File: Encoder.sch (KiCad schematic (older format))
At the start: 7 parts

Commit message: ordenar referencias de componentes
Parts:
- C8, C9: value C -> 1u; Fabricante (none) -> SAMSUNG; Provedor (none) -> TME; Ref (none) -> CL21B105KAFNNNE; Ref_Proveedor (none) -> CL21B105KAFNNNE
- R37: renamed from R36; value R -> 10K; Fabricante (none) -> VISHAY; Potencia (none) -> 1/8W; Provedor (none) -> TME; Ref (none) -> CRCW080510K0FKEA; Ref_Proveedor (none) -> CRCW080510K0FKEA; Tolerancia (none) -> 1%
- R38: renamed from R37; value R -> 10K; Fabricante (none) -> VISHAY; Potencia (none) -> 1/8W; Provedor (none) -> TME; Ref (none) -> CRCW080510K0FKEA; Ref_Proveedor (none) -> CRCW080510K0FKEA; Tolerancia (none) -> 1%
- R39: renamed from R38; value R -> 10K; Fabricante (none) -> VISHAY; Potencia (none) -> 1/8W; Provedor (none) -> TME; Ref (none) -> CRCW080510K0FKEA; Ref_Proveedor (none) -> CRCW080510K0FKEA; Tolerancia (none) -> 1%
- R40: renamed from R39; value R -> 10K; Fabricante (none) -> VISHAY; Potencia (none) -> 1/8W; Provedor (none) -> TME; Ref (none) -> CRCW080510K0FKEA; Ref_Proveedor (none) -> CRCW080510K0FKEA; Tolerancia (none) -> 1%
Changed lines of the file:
@@
 $Descr User 8268 5846
 encoding utf-8
-Sheet 14 15
+Sheet 15 15
 Title ""
 Date ""
@@
 	1600 2450 1600 2750
 $Comp
-L GND #PWR052
+L GND #PWR57
 U 1 1 579DF9A7
 P 1600 2750
-F 0 "#PWR052" H 1600 2500 50  0001 C CNN
+F 0 "#PWR57" H 1600 2500 50  0001 C CNN
 F 1 "GND" H 1605 2577 50  0000 C CNN
 F 2 "" H 1600 2750 50  0000 C CNN
@@
 $EndComp
 $Comp
-L R R36
+L R R37
 U 1 1 579DF9C8
 P 2400 1800
-F 0 "R36" H 2470 1846 50  0000 L CNN
-F 1 "R" H 2470 1755 50  0000 L CNN
+F 0 "R37" H 2470 1846 50  0000 L CNN
+F 1 "10K" H 2470 1755 50  0000 L CNN
 F 2 "Resistors_SMD:R_0805" V 2330 1800 50  0001 C CNN
 F 3 "" H 2400 1800 50  0000 C CNN
+F 4 "VISHAY" H 3950 1650 60  0001 C CNN "Fabricante"
+F 5 "CRCW080510K0FKEA" H 3950 1650 60  0001 C CNN "Ref"
+F 6 "1/8W" H 3950 1650 60  0001 C CNN "Potencia"
+F 7 "1%" H 3950 1650 60  0001 C CNN "Tolerancia"
+F 8 "TME" H 3950 1650 60  0001 C CNN "Provedor"
+F 9 "CRCW080510K0FKEA" H 3950 1650 60  0001 C CNN "Ref_Proveedor"
 	1    2400 1800
 	1    0    0    -1
 $EndComp
 $Comp
-L R R38
+L R R39
 U 1 1 579DFA38
 P 2750 1800
-F 0 "R38" H 2820 1846 50  0000 L CNN
-F 1 "R" H 2820 1755 50  0000 L CNN
+F 0 "R39" H 2820 1846 50  0000 L CNN
+F 1 "10K" H 2820 1755 50  0000 L CNN
 F 2 "Resistors_SMD:R_0805" V 2680 1800 50  0001 C CNN
 F 3 "" H 2750 1800 50  0000 C CNN
+F 4 "VISHAY" H 3950 1650 60  0001 C CNN "Fabricante"
+F 5 "CRCW080510K0FKEA" H 3950 1650 60  0001 C CNN "Ref"
+F 6 "1/8W" H 3950 1650 60  0001 C CNN "Potencia"
+F 7 "1%" H 3950 1650 60  0001 C CNN "Tolerancia"
+F 8 "TME" H 3950 1650 60  0001 C CNN "Provedor"
+F 9 "CRCW080510K0FKEA" H 3950 1650 60  0001 C CNN "Ref_Proveedor"
 	1    2750 1800
 	1    0    0    -1
 $EndComp
 $Comp
-L R R37
+L R R38
 U 1 1 579DFA57
 P 2400 2450
-F 0 "R37" H 2470 2496 50  0000 L CNN
-F 1 "R" H 2470 2405 50  0000 L CNN
+F 0 "R38" H 2470 2496 50  0000 L CNN
+F 1 "10K" H 2470 2405 50  0000 L CNN
 F 2 "Resistors_SMD:R_0805" V 2330 2450 50  0001 C CNN
 F 3 "" H 2400 2450 50  0000 C CNN
+F 4 "VISHAY" H 3950 1650 60  0001 C CNN "Fabricante"
+F 5 "CRCW080510K0FKEA" H 3950 1650 60  0001 C CNN "Ref"
+F 6 "1/8W" H 3950 1650 60  0001 C CNN "Potencia"
+F 7 "1%" H 3950 1650 60  0001 C CNN "Tolerancia"
+F 8 "TME" H 3950 1650 60  0001 C CNN "Provedor"
+F 9 "CRCW080510K0FKEA" H 3950 1650 60  0001 C CNN "Ref_Proveedor"
 	1    2400 2450
 	1    0    0    -1
 $EndComp
 $Comp
-L R R39
+L R R40
 U 1 1 579DFA8F
 P 2750 2450
-F 0 "R39" H 2820 2496 50  0000 L CNN
-F 1 "R" H 2820 2405 50  0000 L CNN
+F 0 "R40" H 2820 2496 50  0000 L CNN
+F 1 "10K" H 2820 2405 50  0000 L CNN
 F 2 "Resistors_SMD:R_0805" V 2680 2450 50  0001 C CNN
 F 3 "" H 2750 2450 50  0000 C CNN
+F 4 "VISHAY" H 3950 1650 60  0001 C CNN "Fabricante"
+F 5 "CRCW080510K0FKEA" H 3950 1650 60  0001 C CNN "Ref"
+F 6 "1/8W" H 3950 1650 60  0001 C CNN "Potencia"
+F 7 "1%" H 3950 1650 60  0001 C CNN "Tolerancia"
+F 8 "TME" H 3950 1650 60  0001 C CNN "Provedor"
+F 9 "CRCW080510K0FKEA" H 3950 1650 60  0001 C CNN "Ref_Proveedor"
 	1    2750 2450
 	1    0    0    -1
@@
 P 2400 3100
 F 0 "C8" H 2515 3146 50  0000 L CNN
-F 1 "C" H 2515 3055 50  0000 L CNN
+F 1 "1u" H 2515 3055 50  0000 L CNN
 F 2 "Capacitors_SMD:C_0805" H 2438 2950 50  0001 C CNN
 F 3 "" H 2400 3100 50  0000 C CNN
+F 4 "SAMSUNG" H 2400 3100 60  0001 C CNN "Fabricante"
+F 5 "CL21B105KAFNNNE" H 2400 3100 60  0001 C CNN "Ref"
+F 6 "~" H 2400 3100 60  0001 C CNN "Potencia"
+F 7 "~" H 2400 3100 60  0001 C CNN "Tolerancia"
+F 8 "TME" H 2400 3100 60  0001 C CNN "Provedor"
+F 9 "CL21B105KAFNNNE" H 2400 3100 60  0001 C CNN "Ref_Proveedor"
 	1    2400 3100
 	1    0    0    -1
@@
 P 2750 3100
 F 0 "C9" H 2865 3146 50  0000 L CNN
-F 1 "C" H 2865 3055 50  0000 L CNN
+F 1 "1u" H 2865 3055 50  0000 L CNN
 F 2 "Capacitors_SMD:C_0805" H 2788 2950 50  0001 C CNN
 F 3 "" H 2750 3100 50  0000 C CNN
+F 4 "SAMSUNG" H 2750 3100 60  0001 C CNN "Fabricante"
+F 5 "CL21B105KAFNNNE" H 2750 3100 60  0001 C CNN "Ref"
+F 6 "~" H 2750 3100 60  0001 C CNN "Potencia"
+F 7 "~" H 2750 3100 60  0001 C CNN "Tolerancia"
+F 8 "TME" H 2750 3100 60  0001 C CNN "Provedor"
+F 9 "CL21B105KAFNNNE" H 2750 3100 60  0001 C CNN "Ref_Proveedor"
 	1    2750 3100
 	1    0    0    -1
@@
 	2400 2600 2400 2950
 $Comp
-L GND #PWR053
+L GND #PWR59
 U 1 1 579DFBCA
 P 2400 3350
-F 0 "#PWR053" H 2400 3100 50  0001 C CNN
+F 0 "#PWR59" H 2400 3100 50  0001 C CNN
 F 1 "GND" H 2405 3177 50  0000 C CNN
 F 2 "" H 2400 3350 50  0000 C CNN
@@
 $EndComp
 $Comp
-L GND #PWR054
+L GND #PWR61
 U 1 1 579DFBEA
 P 2750 3350
-F 0 "#PWR054" H 2750 3100 50  0001 C CNN
+F 0 "#PWR61" H 2750 3100 50  0001 C CNN
 F 1 "GND" H 2755 3177 50  0000 C CNN
 F 2 "" H 2750 3350 50  0000 C CNN
@@
 	2400 3350 2400 3250
 $Comp
-L +5V #PWR055
+L +5V #PWR58
 U 1 1 579DFC2A
 P 2400 1450
-F 0 "#PWR055" H 2400 1300 50  0001 C CNN
+F 0 "#PWR58" H 2400 1300 50  0001 C CNN
 F 1 "+5V" H 2415 1623 50  0000 C CNN
 F 2 "" H 2400 1450 50  0000 C CNN
@@
 $EndComp
 $Comp
-L +5V #PWR056
+L +5V #PWR60
 U 1 1 579DFC51
 P 2750 1450
-F 0 "#PWR056" H 2750 1300 50  0001 C CNN
+F 0 "#PWR60" H 2750 1300 50  0001 C CNN
 F 1 "+5V" H 2765 1623 50  0000 C CNN
 F 2 "" H 2750 1450 50  0000 C CNN

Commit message: cambiados encoder y potenciometro
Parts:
- B1: footprint Sensores:Bourns_3315C_encoder_incremental -> Sensores:ALPS_EC12E24_encoder_incremental; Fabricante Bourns -> ALPS; Ref 3315C-101-016L -> EC12E24202A2; Ref_Proveedor 827-5019 -> 623-4215
- R37, R38, R39, R40: footprint Resistors_SMD:R_0805 -> Resistencias:R_0805
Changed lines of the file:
@@
 F 0 "B1" H 1656 2877 100 0000 C CNN
 F 1 "Encoder_Inc" H 1656 2711 100 0000 C CNN
-F 2 "Sensores:Bourns_3315C_encoder_incremental" H 1450 2250 100 0001 C CNN
+F 2 "Sensores:ALPS_EC12E24_encoder_incremental" H 1450 2250 100 0001 C CNN
 F 3 "" H 1450 2250 100 0001 C CNN
-F 4 "Bourns" H 1600 2250 60  0001 C CNN "Fabricante"
-F 5 "3315C-101-016L" H 1600 2250 60  0001 C CNN "Ref"
+F 4 "ALPS" H 1600 2250 60  0001 C CNN "Fabricante"
+F 5 "EC12E24202A2" H 1600 2250 60  0001 C CNN "Ref"
 F 6 "~" H 1600 2250 60  0001 C CNN "Potencia"
 F 7 "~" H 1600 2250 60  0001 C CNN "Tolerancia"
 F 8 "RS" H 1600 2250 60  0001 C CNN "Provedor"
-F 9 "827-5019" H 1600 2250 60  0001 C CNN "Ref_Proveedor"
+F 9 "623-4215" H 1600 2250 60  0001 C CNN "Ref_Proveedor"
 	1    1600 2250
 	1    0    0    -1
@@
 	1600 2450 1600 2750
 $Comp
-L GND #PWR57
+L GND #PWR059
 U 1 1 579DF9A7
 P 1600 2750
-F 0 "#PWR57" H 1600 2500 50  0001 C CNN
+F 0 "#PWR059" H 1600 2500 50  0001 C CNN
 F 1 "GND" H 1605 2577 50  0000 C CNN
 F 2 "" H 1600 2750 50  0000 C CNN
@@
 F 0 "R37" H 2470 1846 50  0000 L CNN
 F 1 "10K" H 2470 1755 50  0000 L CNN
-F 2 "Resistors_SMD:R_0805" V 2330 1800 50  0001 C CNN
+F 2 "Resistencias:R_0805" V 2330 1800 50  0001 C CNN
 F 3 "" H 2400 1800 50  0000 C CNN
 F 4 "VISHAY" H 3950 1650 60  0001 C CNN "Fabricante"
@@
 F 0 "R39" H 2820 1846 50  0000 L CNN
 F 1 "10K" H 2820 1755 50  0000 L CNN
-F 2 "Resistors_SMD:R_0805" V 2680 1800 50  0001 C CNN
+F 2 "Resistencias:R_0805" V 2680 1800 50  0001 C CNN
 F 3 "" H 2750 1800 50  0000 C CNN
 F 4 "VISHAY" H 3950 1650 60  0001 C CNN "Fabricante"
@@
 F 0 "R38" H 2470 2496 50  0000 L CNN
 F 1 "10K" H 2470 2405 50  0000 L CNN
-F 2 "Resistors_SMD:R_0805" V 2330 2450 50  0001 C CNN
+F 2 "Resistencias:R_0805" V 2330 2450 50  0001 C CNN
 F 3 "" H 2400 2450 50  0000 C CNN
 F 4 "VISHAY" H 3950 1650 60  0001 C CNN "Fabricante"
@@
 F 0 "R40" H 2820 2496 50  0000 L CNN
 F 1 "10K" H 2820 2405 50  0000 L CNN
-F 2 "Resistors_SMD:R_0805" V 2680 2450 50  0001 C CNN
+F 2 "Resistencias:R_0805" V 2680 2450 50  0001 C CNN
 F 3 "" H 2750 2450 50  0000 C CNN
 F 4 "VISHAY" H 3950 1650 60  0001 C CNN "Fabricante"
@@
 	2400 2600 2400 2950
 $Comp
-L GND #PWR59
+L GND #PWR060
 U 1 1 579DFBCA
 P 2400 3350
-F 0 "#PWR59" H 2400 3100 50  0001 C CNN
+F 0 "#PWR060" H 2400 3100 50  0001 C CNN
 F 1 "GND" H 2405 3177 50  0000 C CNN
 F 2 "" H 2400 3350 50  0000 C CNN
@@
 $EndComp
 $Comp
-L GND #PWR61
+L GND #PWR061
 U 1 1 579DFBEA
 P 2750 3350
-F 0 "#PWR61" H 2750 3100 50  0001 C CNN
+F 0 "#PWR061" H 2750 3100 50  0001 C CNN
 F 1 "GND" H 2755 3177 50  0000 C CNN
 F 2 "" H 2750 3350 50  0000 C CNN
@@
 	2400 3350 2400 3250
 $Comp
-L +5V #PWR58
+L +5V #PWR062
 U 1 1 579DFC2A
 P 2400 1450
-F 0 "#PWR58" H 2400 1300 50  0001 C CNN
+F 0 "#PWR062" H 2400 1300 50  0001 C CNN
 F 1 "+5V" H 2415 1623 50  0000 C CNN
 F 2 "" H 2400 1450 50  0000 C CNN
@@
 $EndComp
 $Comp
-L +5V #PWR60
+L +5V #PWR063
 U 1 1 579DFC51
 P 2750 1450
-F 0 "#PWR60" H 2750 1300 50  0001 C CNN
+F 0 "#PWR063" H 2750 1300 50  0001 C CNN
 F 1 "+5V" H 2765 1623 50  0000 C CNN
 F 2 "" H 2750 1450 50  0000 C CNN

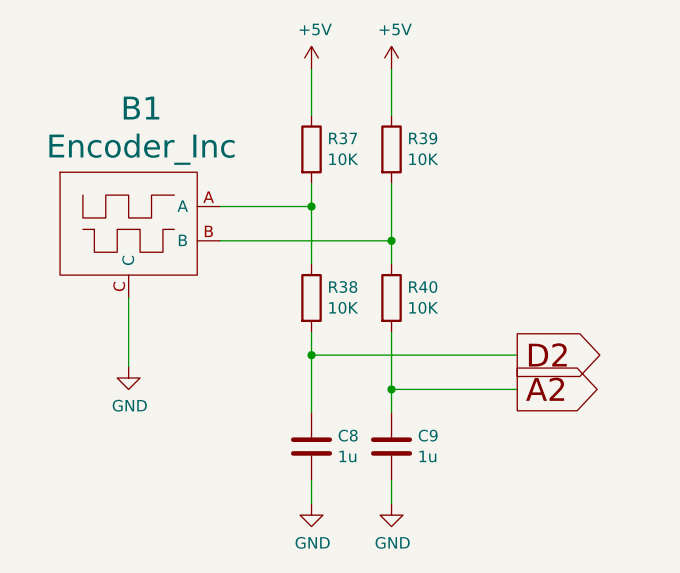
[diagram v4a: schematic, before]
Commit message: añadidos driver para led y conectores para fotodiodos infrarrojos
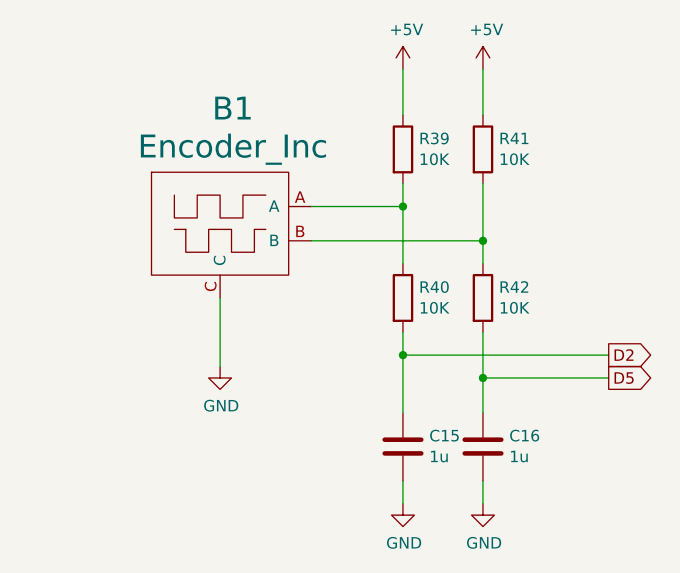
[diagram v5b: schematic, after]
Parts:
- renumbered C8 to C15, C9 to C16, R37 to R39, R38 to R40, R39 to R41, R40 to R42
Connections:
- net A2 renamed D5
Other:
- moved on the sheet: B1, C15, C16, R39, R40, R41, R42
